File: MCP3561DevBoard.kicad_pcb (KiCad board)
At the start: 2 copper layers, 81.3 x 66 mm, 52 parts, among them J1 Conn_Coaxial, J2 Conn_Coaxial, J3 Conn_02x03_Counter_Clockwise, J4 Conn_02x03_Counter_Clockwise, J5 Conn_01x04, J6 Conn_02x03_Counter_Clockwise, J7 Conn_01x10_Male, J8 Screw_Terminal_01x02, U3 TLV9051, U4 ADR366, U5 ADP3330-X, U6 ADP3330-X, U7 MCP3561, U8 Teensy4.1

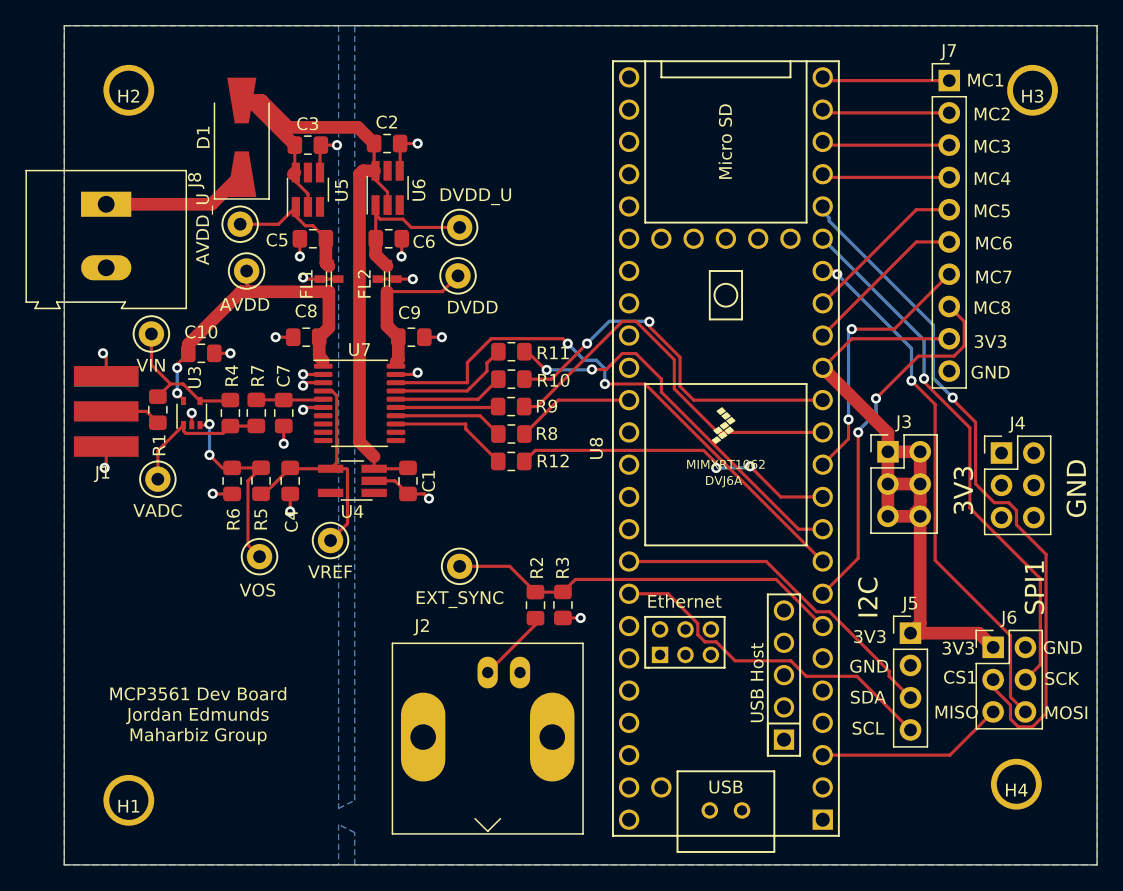
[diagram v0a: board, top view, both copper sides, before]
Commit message: fixed power plane so that it contains voltage reference
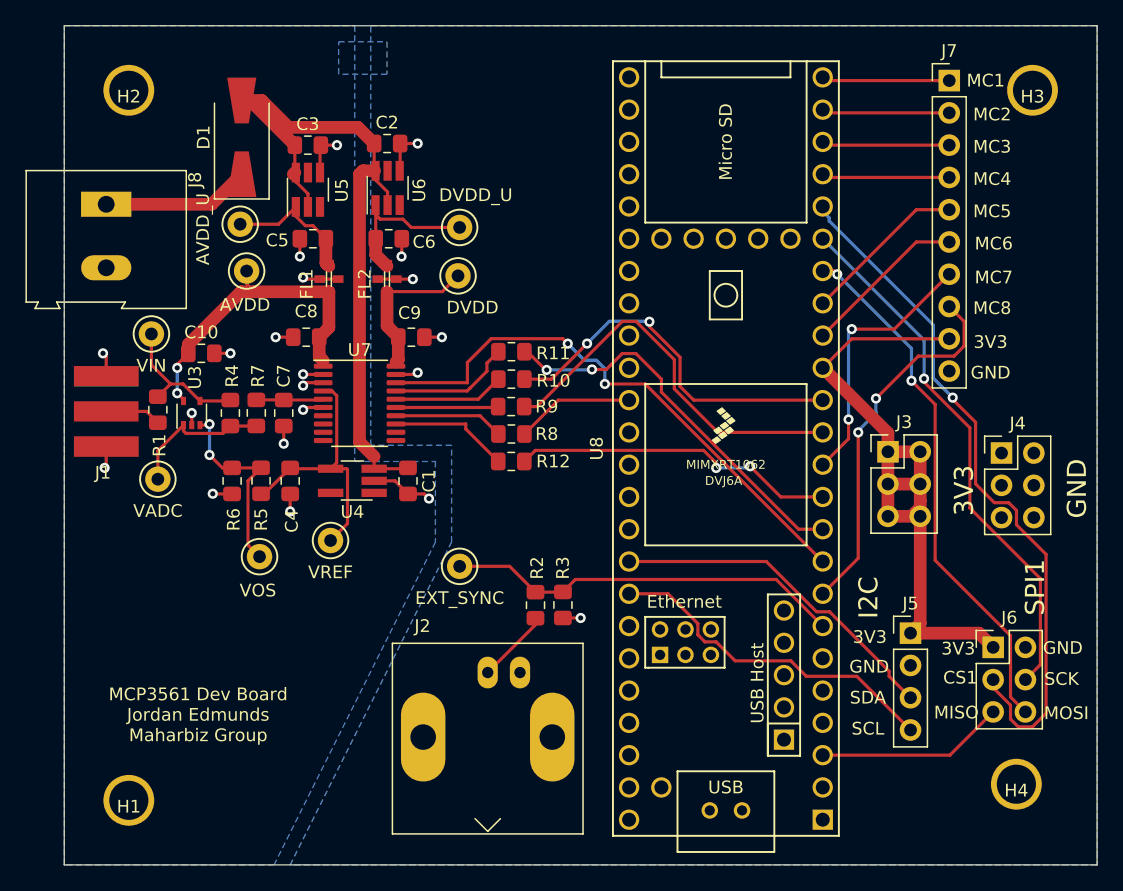
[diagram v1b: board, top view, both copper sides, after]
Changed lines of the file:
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@@
     (polygon
       (pts
-        (xy 113.03 95.885) (xy 114.3 95.25) (xy 114.3 34.29) (xy 172.72 34.29) (xy 172.72 100.33)
-        (xy 114.3 100.33) (xy 114.3 97.79) (xy 113.03 97.155) (xy 113.03 100.33) (xy 91.44 100.33)
-        (xy 91.44 34.29) (xy 113.03 34.29)
+        (xy 114.3 68.58) (xy 120.65 68.58) (xy 120.65 74.93) (xy 107.95 100.33) (xy 91.44 100.33)
+        (xy 91.44 34.29) (xy 114.3 34.29)
       )
     )
+  )
+  (zone (net 1) (net_name GND) (layer B.Cu) (hatch edge 0.508)
+    (connect_pads (clearance 0.508))
+    (min_thickness 0.254)
+    (fill yes (arc_segments 32) (thermal_gap 0.508) (thermal_bridge_width 0.508))
+    (polygon
+      (pts
+        (xy 172.72 100.33) (xy 109.22 100.33) (xy 121.92 74.93) (xy 121.92 67.31) (xy 115.57 67.31)
+        (xy 115.57 34.29) (xy 172.72 34.29)
+      )
+    )
+  )
+  (zone (net 1) (net_name GND) (layer B.Cu) (hatch edge 0.508)
+    (connect_pads (clearance 0.508))
+    (min_thickness 0.254)
+    (fill yes (arc_segments 32) (thermal_gap 0.508) (thermal_bridge_width 0.508))
+    (polygon
+      (pts
+        (xy 116.84 38.1) (xy 113.03 38.1) (xy 113.03 35.56) (xy 116.84 35.56)
+      )
+    )
